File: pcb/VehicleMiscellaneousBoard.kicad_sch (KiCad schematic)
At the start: 5 parts, among them J1 Conn_01x17, J2 Conn_01x17, U1 OpenMV H7+, U2 Seeed_Studio_XIAO-ESP32-S3-Se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

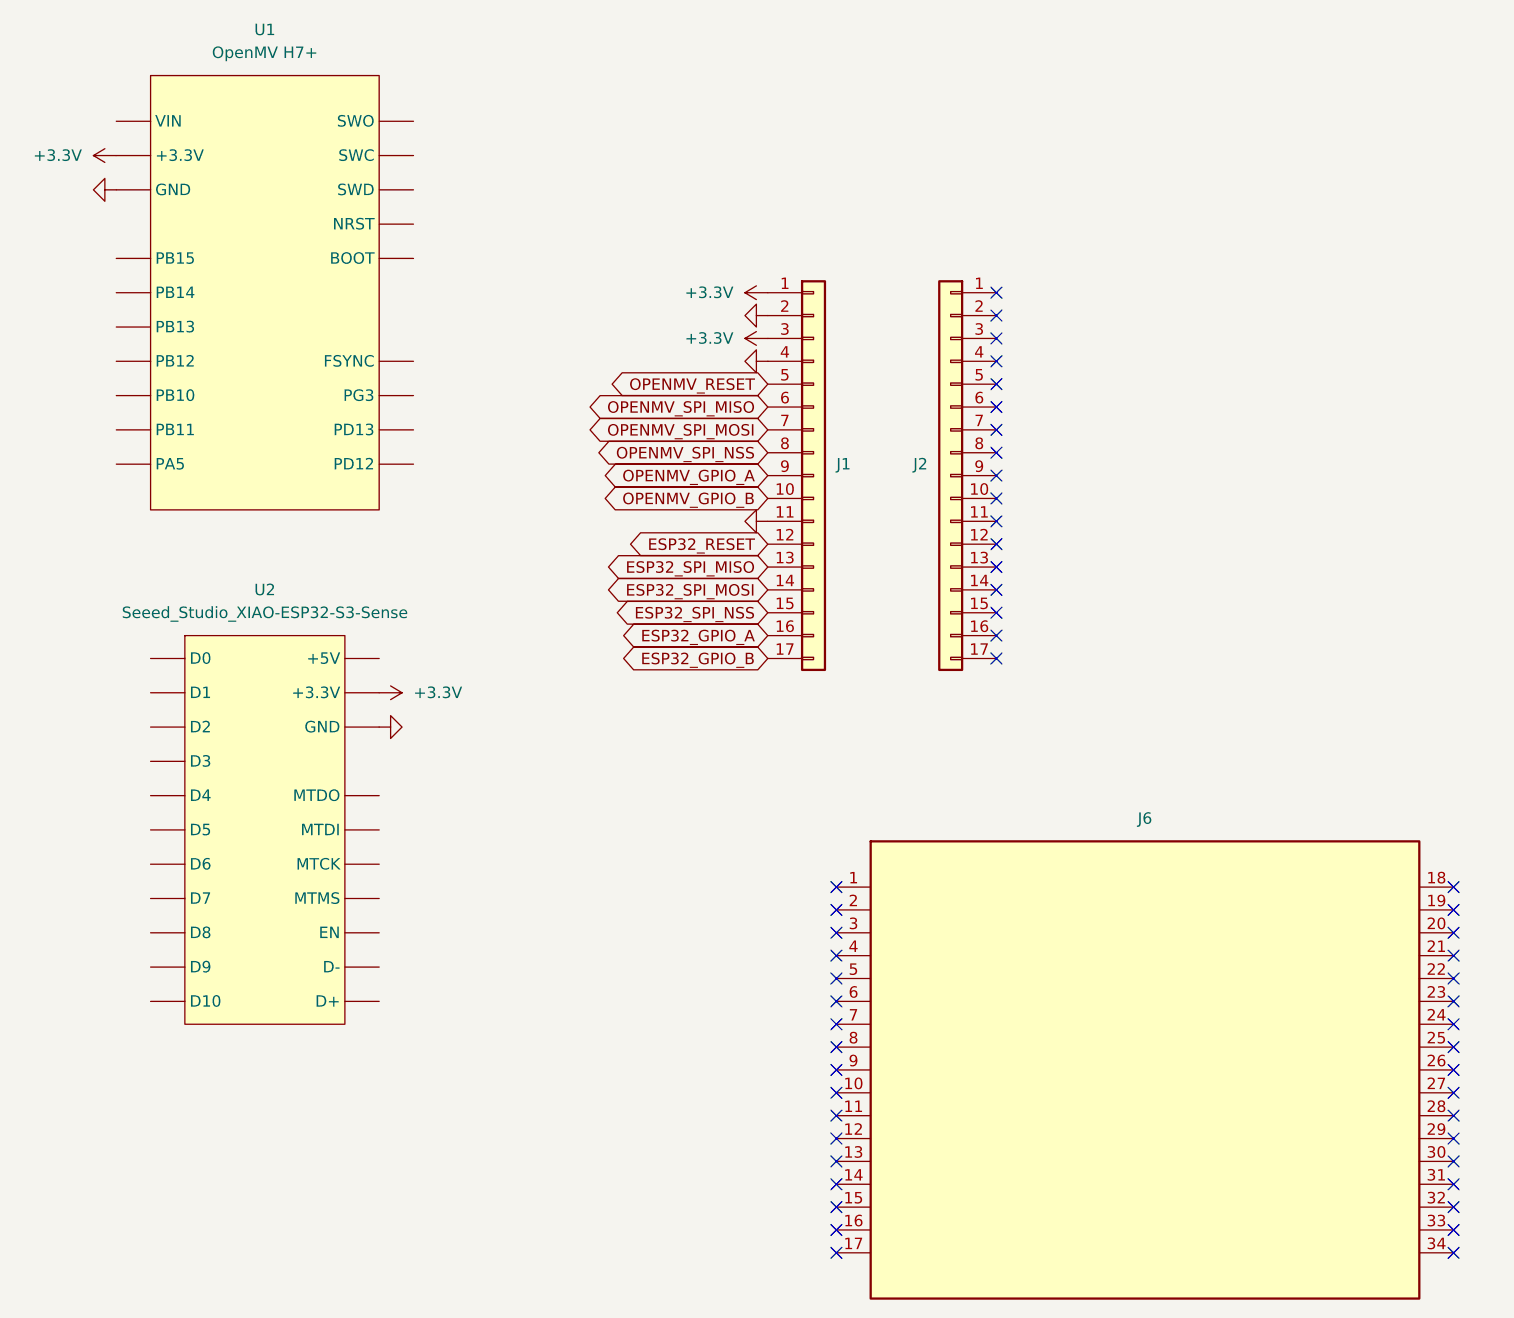
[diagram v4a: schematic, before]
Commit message: Updated `VehicleStackConnector` with pin usages.
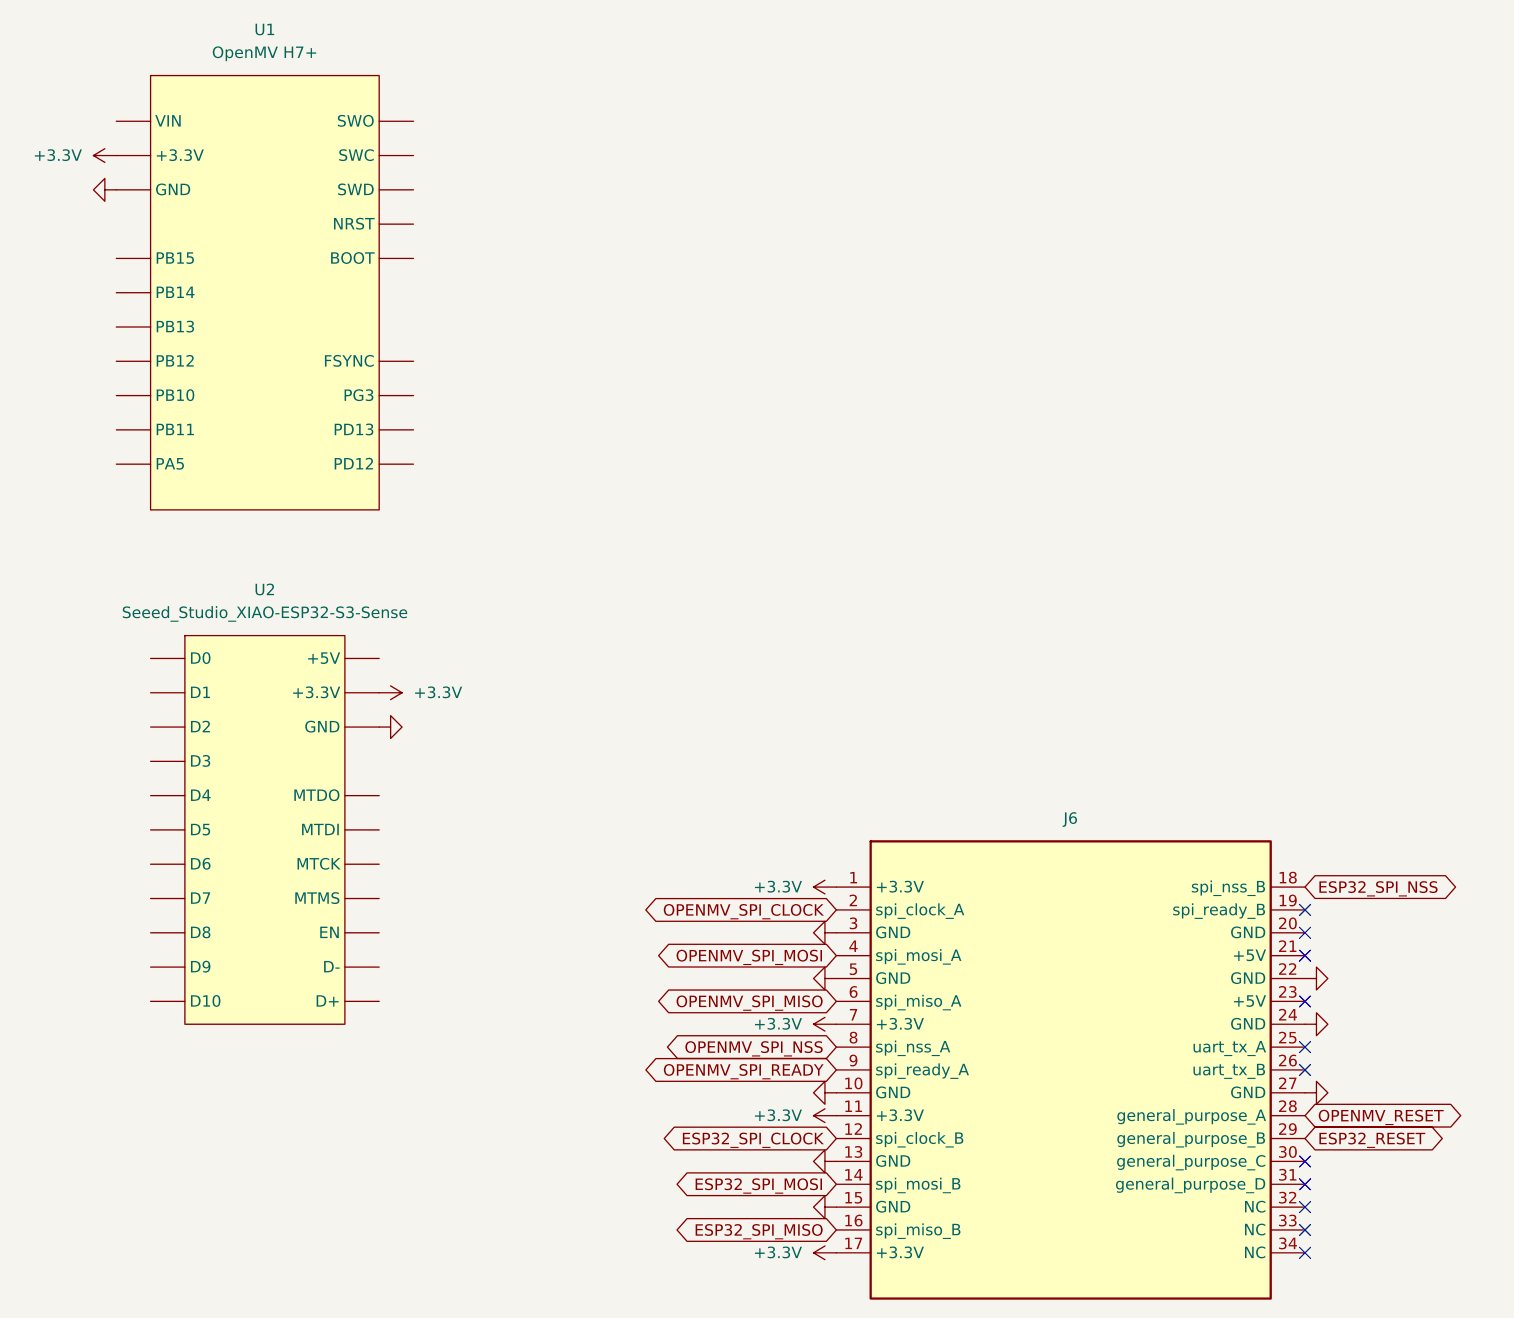
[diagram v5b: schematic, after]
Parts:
- removed J1, J2: Conn_01x17, Connector_PinSocket_2.54mm:PinSocket_1x17_P2.54mm_Vertical, symbol Connector_Generic:Conn_01x17
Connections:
- net +3.3V: now also J6.1 (+3.3V), J6.11 (+3.3V), J6.17 (+3.3V), J6.7 (+3.3V)
- net ESP32_RESET: now also J6.29 (general_purpose_B)
- net ESP32_SPI_MISO: now also J6.16 (spi_miso_B)
- net ESP32_SPI_MOSI: now also J6.14 (spi_mosi_B)
- net ESP32_SPI_NSS: now also J6.18 (spi_nss_B)
- net GND: now also J6.10 (GND), J6.13 (GND), J6.15 (GND), J6.22 (GND), J6.24 (GND), J6.27 (GND), J6.3 (GND), J6.5 (GND)
- net OPENMV_RESET: now also J6.28 (general_purpose_A)
- net OPENMV_SPI_MISO: now also J6.6 (spi_miso_A)
- net OPENMV_SPI_MOSI: now also J6.4 (spi_mosi_A)
- net OPENMV_SPI_NSS: now also J6.8 (spi_nss_A)
- net ESP32_SPI_CLOCK: now reaches J6.12 (spi_clock_B)
- net OPENMV_SPI_CLOCK: now reaches J6.2 (spi_clock_A)
- net OPENMV_SPI_READY: now reaches J6.9 (spi_ready_A)
- no-connect marks 51 -> 11

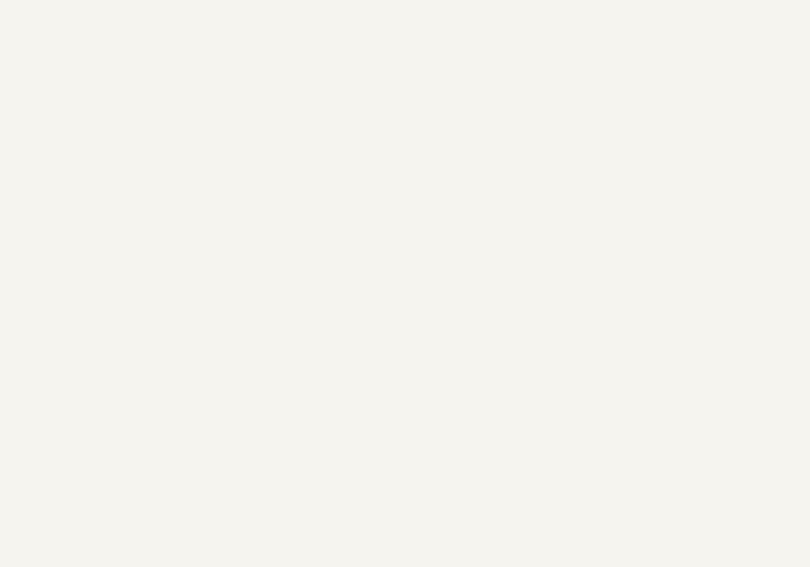
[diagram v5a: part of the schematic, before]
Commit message: Added connector for VN-100 on `VehicleMiscellaneousBoard`.
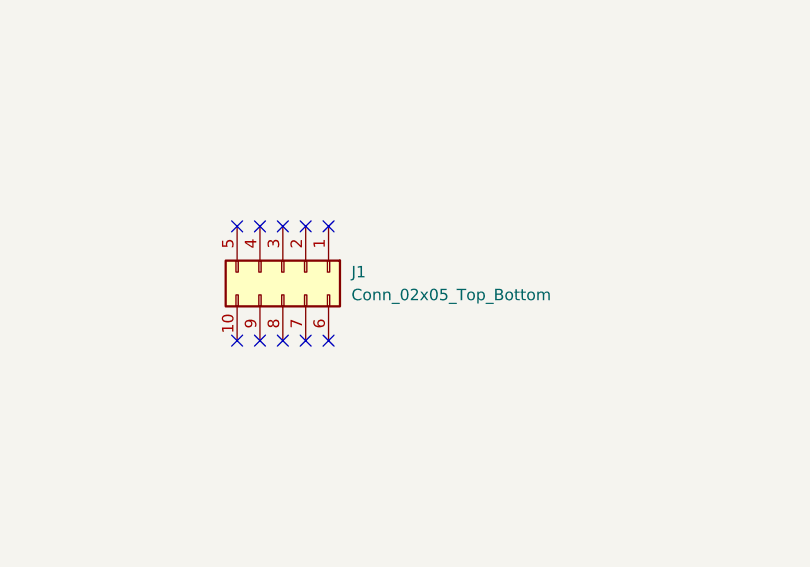
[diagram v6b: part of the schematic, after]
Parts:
- added J1: Conn_02x05_Top_Bottom, Connector_JST:JST_XH_B10B-XH-A_1x10_P2.50mm_Vertical, symbol Connector_Generic:Conn_02x05_Top_Bottom
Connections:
- no-connect marks 11 -> 21
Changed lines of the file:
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@@
 	(paper "A4")
 	(no_connect
+		(at 161.29 80.01)
+	)
+	(no_connect
 		(at 224.79 176.53)
 	)
@@
 	)
 	(no_connect
+		(at 168.91 92.71)
+	)
+	(no_connect
 		(at 224.79 179.07)
 	)
 	(no_connect
+		(at 163.83 80.01)
+	)
+	(no_connect
+		(at 166.37 92.71)
+	)
+	(no_connect
+		(at 171.45 92.71)
+	)
+	(no_connect
 		(at 224.79 153.67)
 	)
@@
 	)
 	(no_connect
+		(at 168.91 80.01)
+	)
+	(no_connect
 		(at 224.79 173.99)
 	)
 	(no_connect
+		(at 166.37 80.01)
+	)
+	(no_connect
+		(at 163.83 92.71)
+	)
+	(no_connect
+		(at 161.29 92.71)
+	)
+	(no_connect
 		(at 224.79 143.51)
 	)
@@
 	(no_connect
 		(at 224.79 171.45)
+	)
+	(no_connect
+		(at 171.45 80.01)
 	)
 	(global_label "ESP32_SPI_MOSI"
@@
 					(unit 1)
 				)
+			)
+		)
+	)
+	(symbol
+		(lib_id "Connector_Generic:Conn_02x05_Top_Bottom")
+		(at 166.37 85.09 270)
+		(unit 1)
+		(exclude_from_sim no)
+		(in_bom yes)
+		(on_board yes)
+		(dnp no)
+		(fields_autoplaced yes)
+		(property "Reference" "J1"
+			(at 173.99 85.0899 90)
+			(effects
+				(font
+					(size 1.27 1.27)
+				)
+				(justify left)
+			)
+		)
+		(property "Value" "Conn_02x05_Top_Bottom"
+			(at 173.99 87.6299 90)
+			(effects
+				(font
+					(size 1.27 1.27)
+				)
+				(justify left)
+			)
+		)
+		(property "Footprint" "Connector_JST:JST_XH_B10B-XH-A_1x10_P2.50mm_Vertical"
+			(at 166.37 85.09 0)
+			(effects
+				(font
+					(size 1.27 1.27)
+				)
+				(hide yes)
+			)
+		)
+		(property "Datasheet" "~"
+			(at 166.37 85.09 0)
+			(effects
+				(font
+					(size 1.27 1.27)
+				)
+				(hide yes)
+			)
+		)
+		(property "Description" "Generic connector, double row, 02x05, top/bottom pin numbering scheme (row 1: 1...pins_per_row, row2: pins_per_row+1 ... num_pins), script generated (kicad-library-utils/schlib/autogen/connector/)"
+			(at 166.37 85.09 0)
+			(effects
+				(font
+					(size 1.27 1.27)
+				)
+				(hide yes)
+			)
+		)
+		(pin "9"
+		)
+		(pin "2"
+		)
+		(pin "1"
+		)
+		(pin "10"
+		)
+		(pin "7"
+		)
+		(pin "6"
+		)
+		(pin "5"
+		)
+		(pin "4"
+		)
+		(pin "3"
+		)
+		(pin "8"
+		)
+		(instances
+			(project ""
+				(path "/091a7226-d417-4b79-83fb-bb50ff9fd5b7"
+					(reference "J1")
+					(unit 1)
+				)

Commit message: Updated vehicle stack-up edge-cuts for `VehicleMiscellaneousBoard` and `VehicleFlightComputer`.
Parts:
- J1: footprint Connector_JST:JST_XH_B10B-XH-A_1x10_P2.50mm_Vertical -> Connector_JST:JST_XH_S10B-XH-A_1x10_P2.50mm_Horizontal
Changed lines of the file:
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@@
 			)
 		)
-		(property "Footprint" "Connector_JST:JST_XH_B10B-XH-A_1x10_P2.50mm_Vertical"
+		(property "Footprint" "Connector_JST:JST_XH_S10B-XH-A_1x10_P2.50mm_Horizontal"
 			(at 166.37 85.09 0)
 			(effects

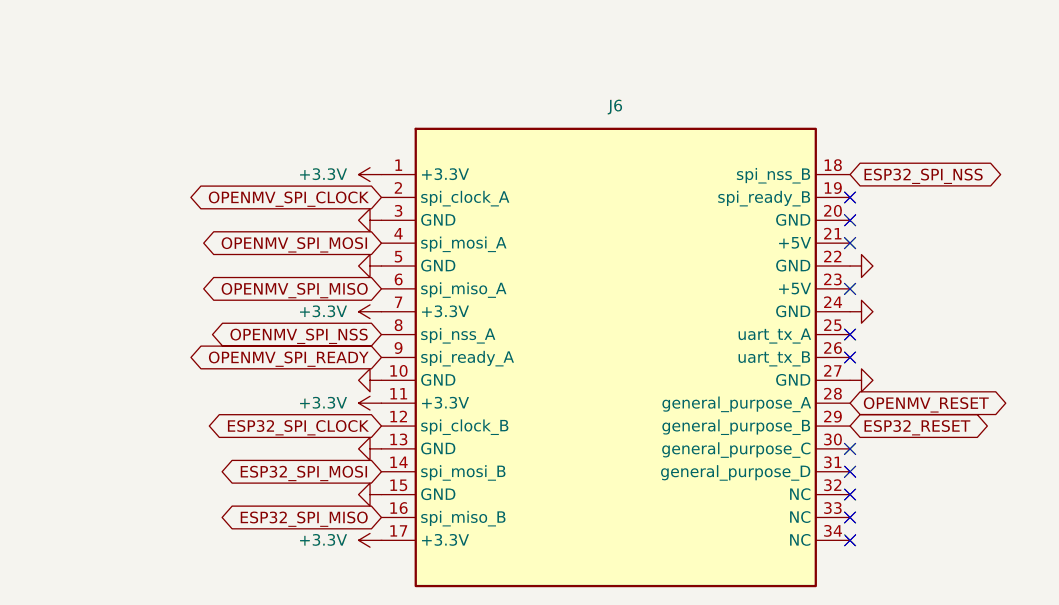
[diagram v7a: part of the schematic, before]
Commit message: Fixed issues reported by `checkPCBs` concerning the stack connectors.
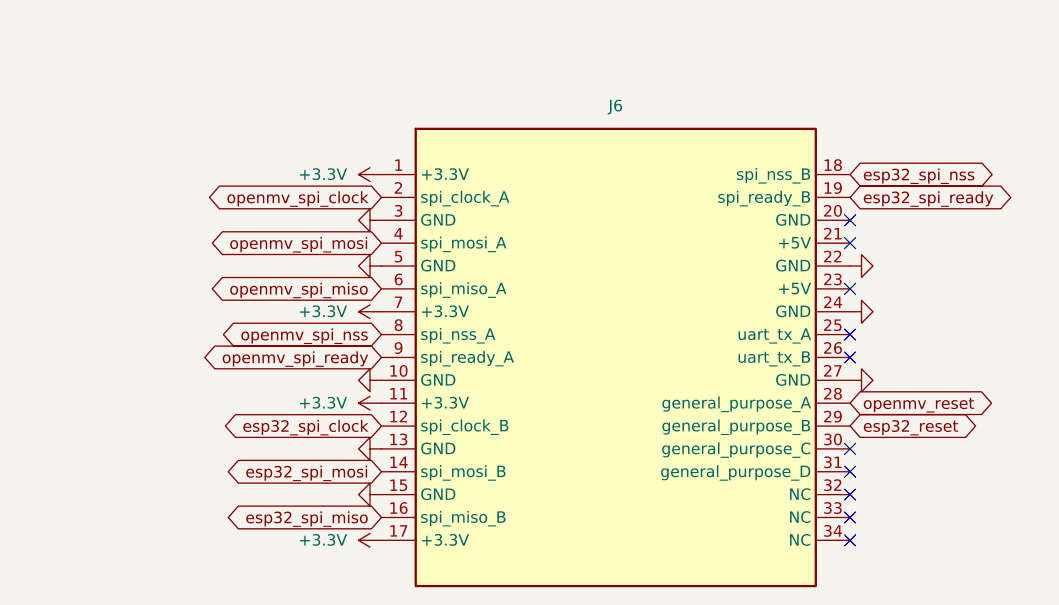
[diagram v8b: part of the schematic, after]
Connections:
- net esp32_spi_ready: now reaches J6.19 (spi_ready_B)
- net ESP32_RESET renamed esp32_reset
- net ESP32_SPI_CLOCK renamed esp32_spi_clock
- net ESP32_SPI_MISO renamed esp32_spi_miso
- net ESP32_SPI_MOSI renamed esp32_spi_mosi
- net ESP32_SPI_NSS renamed esp32_spi_nss
- net OPENMV_RESET renamed openmv_reset
- net OPENMV_SPI_CLOCK renamed openmv_spi_clock
- net OPENMV_SPI_MISO renamed openmv_spi_miso
- net OPENMV_SPI_MOSI renamed openmv_spi_mosi
- net OPENMV_SPI_NSS renamed openmv_spi_nss
- net OPENMV_SPI_READY renamed openmv_spi_ready
- no-connect marks 21 -> 20
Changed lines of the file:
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@@
-	)
-	(no_connect
-		(at 224.79 143.51)
 	)
 	(no_connect
@@
 		(at 171.45 80.01)
 	)
-	(global_label "ESP32_SPI_MOSI"
+	(global_label "esp32_spi_mosi"
 		(shape bidirectional)
 		(at 172.72 173.99 180)
@@
 		)
 		(property "Intersheetrefs" "${INTERSHEET_REFS}"
-			(at 152.9603 173.99 0)
-			(effects
-				(font
-					(size 1.27 1.27)
-				)
-				(justify right)
-				(hide yes)
-			)
-		)
-	)
-	(global_label "OPENMV_SPI_NSS"
+			(at 153.7465 173.99 0)
+			(effects
+				(font
+					(size 1.27 1.27)
+				)
+				(justify right)
+				(hide yes)
+			)
+		)
+	)
+	(global_label "openmv_spi_nss"
 		(shape bidirectional)
 		(at 172.72 158.75 180)
@@
 		)
 		(property "Intersheetrefs" "${INTERSHEET_REFS}"
-			(at 152.2345 158.75 0)
-			(effects
-				(font
-					(size 1.27 1.27)
-				)
-				(justify right)
-				(hide yes)
-			)
-		)
-	)
-	(global_label "OPENMV_RESET"
+			(at 153.5047 158.75 0)
+			(effects
+				(font
+					(size 1.27 1.27)
+				)
+				(justify right)
+				(hide yes)
+			)
+		)
+	)
+	(global_label "openmv_reset"
 		(shape bidirectional)
 		(at 224.79 166.37 0)
@@
 		)
 		(property "Intersheetrefs" "${INTERSHEET_REFS}"
-			(at 243.2192 166.37 0)
-			(effects
-				(font
-					(size 1.27 1.27)
-				)
-				(justify left)
-				(hide yes)
-			)
-		)
-	)
-	(global_label "OPENMV_SPI_MOSI"
+			(at 241.7678 166.37 0)
+			(effects
+				(font
+					(size 1.27 1.27)
+				)
+				(justify left)
+				(hide yes)
+			)
+		)
+	)
+	(global_label "openmv_spi_mosi"
 		(shape bidirectional)
 		(at 172.72 148.59 180)
@@
 		)
 		(property "Intersheetrefs" "${INTERSHEET_REFS}"
-			(at 151.3878 148.59 0)
-			(effects
-				(font
-					(size 1.27 1.27)
-				)
-				(justify right)
-				(hide yes)
-			)
-		)
-	)
-	(global_label "ESP32_SPI_CLOCK"
+			(at 152.2347 148.59 0)
+			(effects
+				(font
+					(size 1.27 1.27)
+				)
+				(justify right)
+				(hide yes)
+			)
+		)
+	)
+	(global_label "esp32_spi_clock"
 		(shape bidirectional)
 		(at 172.72 168.91 180)
@@
 		)
 		(property "Intersheetrefs" "${INTERSHEET_REFS}"
-			(at 151.3879 168.91 0)
-			(effects
-				(font
-					(size 1.27 1.27)
-				)
-				(justify right)
-				(hide yes)
-			)
-		)
-	)
-	(global_label "OPENMV_SPI_READY"
+			(at 153.2022 168.91 0)
+			(effects
+				(font
+					(size 1.27 1.27)
+				)
+				(justify right)
+				(hide yes)
+			)
+		)
+	)
+	(global_label "esp32_spi_nss"
+		(shape bidirectional)
+		(at 224.79 140.97 0)
+		(fields_autoplaced yes)
+		(effects
+			(font
+				(size 1.27 1.27)
+			)
+			(justify left)
+		)
+		(property "Intersheetrefs" "${INTERSHEET_REFS}"
+			(at 242.4935 140.97 0)
+			(effects
+				(font
+					(size 1.27 1.27)
+				)
+				(justify left)
+				(hide yes)
+			)
+		)
+	)
+	(global_label "openmv_spi_ready"
 		(shape bidirectional)
 		(at 172.72 161.29 180)
@@
 		)
 		(property "Intersheetrefs" "${INTERSHEET_REFS}"
-			(at 150.1178 161.29 0)
-			(effects
-				(font
-					(size 1.27 1.27)
-				)
-				(justify right)
-				(hide yes)
-			)
-		)
-	)
-	(global_label "ESP32_RESET"
+			(at 151.5695 161.29 0)
+			(effects
+				(font
+					(size 1.27 1.27)
+				)
+				(justify right)
+				(hide yes)
+			)
+		)
+	)
+	(global_label "esp32_reset"
 		(shape bidirectional)
 		(at 224.79 168.91 0)
@@
 		)
 		(property "Intersheetrefs" "${INTERSHEET_REFS}"
-			(at 241.6467 168.91 0)
-			(effects
-				(font
-					(size 1.27 1.27)
-				)
-				(justify left)
-				(hide yes)
-			)
-		)
-	)
-	(global_label "ESP32_SPI_MISO"
+			(at 240.256 168.91 0)
+			(effects
+				(font
+					(size 1.27 1.27)
+				)
+				(justify left)
+				(hide yes)
+			)
+		)
+	)
+	(global_label "esp32_spi_miso"
 		(shape bidirectional)
 		(at 172.72 179.07 180)
@@
 		)
 		(property "Intersheetrefs" "${INTERSHEET_REFS}"
-			(at 152.9603 179.07 0)
-			(effects
-				(font
-					(size 1.27 1.27)
-				)
-				(justify right)
-				(hide yes)
-			)
-		)
-	)
-	(global_label "ESP32_SPI_NSS"
-		(shape bidirectional)
-		(at 224.79 140.97 0)
-		(fields_autoplaced yes)
-		(effects
-			(font
-				(size 1.27 1.27)
-			)
-			(justify left)
-		)
-		(property "Intersheetrefs" "${INTERSHEET_REFS}"
-			(at 243.703 140.97 0)
-			(effects
-				(font
-					(size 1.27 1.27)
-				)
-				(justify left)
-				(hide yes)
-			)
-		)
-	)
-	(global_label "OPENMV_SPI_CLOCK"
+			(at 153.7465 179.07 0)
+			(effects
+				(font
+					(size 1.27 1.27)
+				)
+				(justify right)
+				(hide yes)
+			)
+		)
+	)
+	(global_label "esp32_spi_ready"
+		(shape bidirectional)
+		(at 224.79 143.51 0)
+		(fields_autoplaced yes)
+		(effects
+			(font
+				(size 1.27 1.27)
+			)
+			(justify left)
+		)
+		(property "Intersheetrefs" "${INTERSHEET_REFS}"
+			(at 244.4287 143.51 0)
+			(effects
+				(font
+					(size 1.27 1.27)
+				)
+				(justify left)
+				(hide yes)
+			)
+		)
+	)
+	(global_label "openmv_spi_clock"
 		(shape bidirectional)
 		(at 172.72 143.51 180)
@@
 		)
 		(property "Intersheetrefs" "${INTERSHEET_REFS}"
-			(at 149.8154 143.51 0)
-			(effects
-				(font
-					(size 1.27 1.27)
-				)
-				(justify right)
-				(hide yes)
-			)
-		)
-	)
-	(global_label "OPENMV_SPI_MISO"
+			(at 151.6904 143.51 0)
+			(effects
+				(font
+					(size 1.27 1.27)
+				)
+				(justify right)
+				(hide yes)
+			)
+		)
+	)
+	(global_label "openmv_spi_miso"
 		(shape bidirectional)
 		(at 172.72 153.67 180)
@@
 		)
 		(property "Intersheetrefs" "${INTERSHEET_REFS}"
-			(at 151.3878 153.67 0)
-			(effects
-				(font
+			(at 152.2347 153.67 0)
+			(effects
+				(font
